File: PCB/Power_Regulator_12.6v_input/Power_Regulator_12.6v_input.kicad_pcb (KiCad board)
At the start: 2 copper layers, 90 x 90 mm, 53 parts, among them J1 SE2-30, U1 TLP3542, U2 TPS55340RTER, U3 TPS563203, U4 TPS54JA20RWWR

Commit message: added test points
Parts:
- added J10: Conn_01x01_Pin, TestPoint:TestPoint_Pad_D1.0mm, F.Cu at (142.4, 80.5)
- added J12: Conn_01x01_Pin, TestPoint:TestPoint_Pad_D1.0mm, F.Cu at (107.7, 95.7)
- added J13: Conn_01x01_Pin, TestPoint:TestPoint_Pad_D1.0mm, F.Cu at (114.5, 90.7)
- added J3: Conn_01x05_Pin, Connector_PinHeader_2.54mm:PinHeader_1x05_P2.54mm_Vertical, F.Cu at (178.5, 119.0)
- added J4: Conn_01x01_Pin, TestPoint:TestPoint_Pad_D1.0mm, F.Cu at (141.8, 73.4)
- added J5: Conn_01x01_Pin, TestPoint:TestPoint_Pad_D1.0mm, F.Cu at (150.0, 88.6)
- added J6: Conn_01x01_Pin, TestPoint:TestPoint_Pad_D1.0mm, F.Cu at (115.8, 107.0)
- added J7: Conn_01x01_Pin, TestPoint:TestPoint_Pad_D1.0mm, F.Cu at (120.0, 99.8)
- added J8: Conn_01x01_Pin, TestPoint:TestPoint_Pad_D1.0mm, F.Cu at (148.0, 68.2)
- added J9: Conn_01x01_Pin, TestPoint:TestPoint_Pad_D1.0mm, F.Cu at (151.4, 107.8)
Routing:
- net +5V: track 66.7 -> 151.0 mm
- net +BATT: track 95.0 -> 161.1 mm
- net /24V_RAW: track 24.1 -> 87.8 mm
- net +3.3VA: track 125.7 -> 170.5 mm
- net Net-(J12-Pin_1): track 3.46 -> 5.79 mm

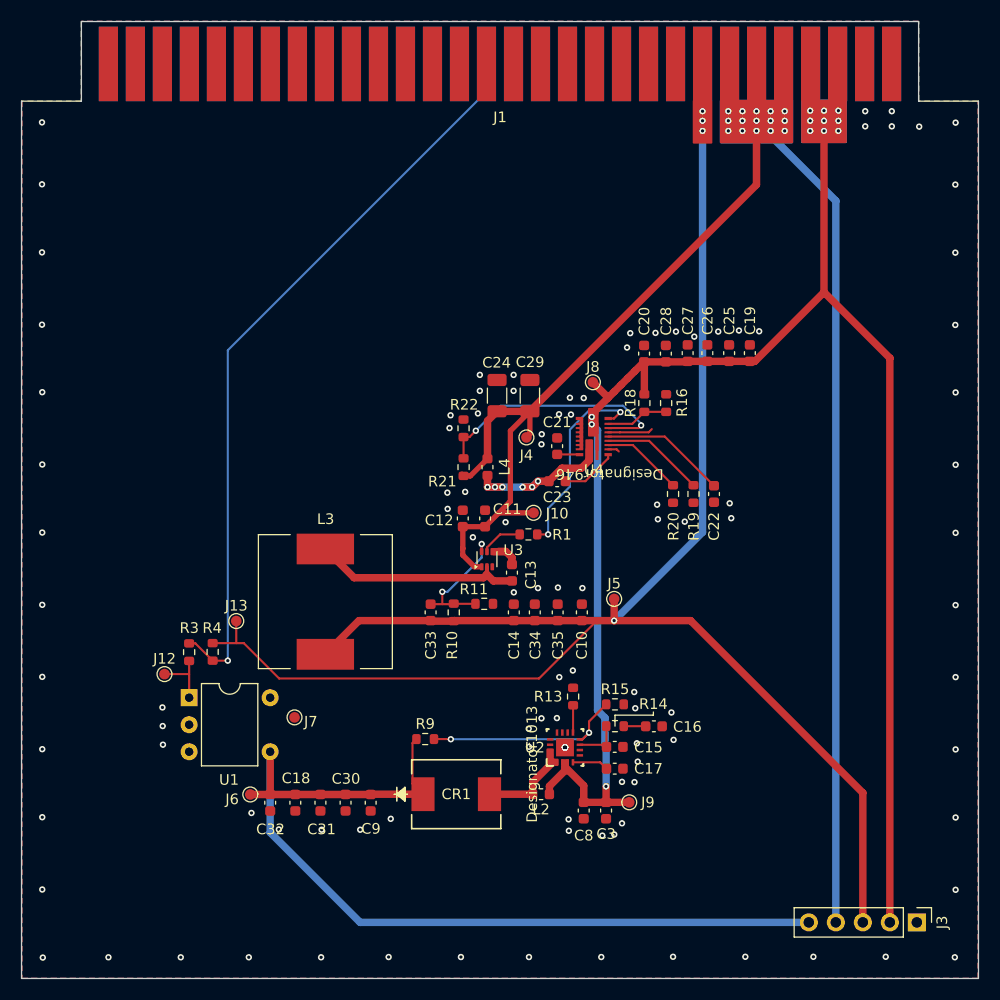
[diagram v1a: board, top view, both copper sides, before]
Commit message: added connector and switch
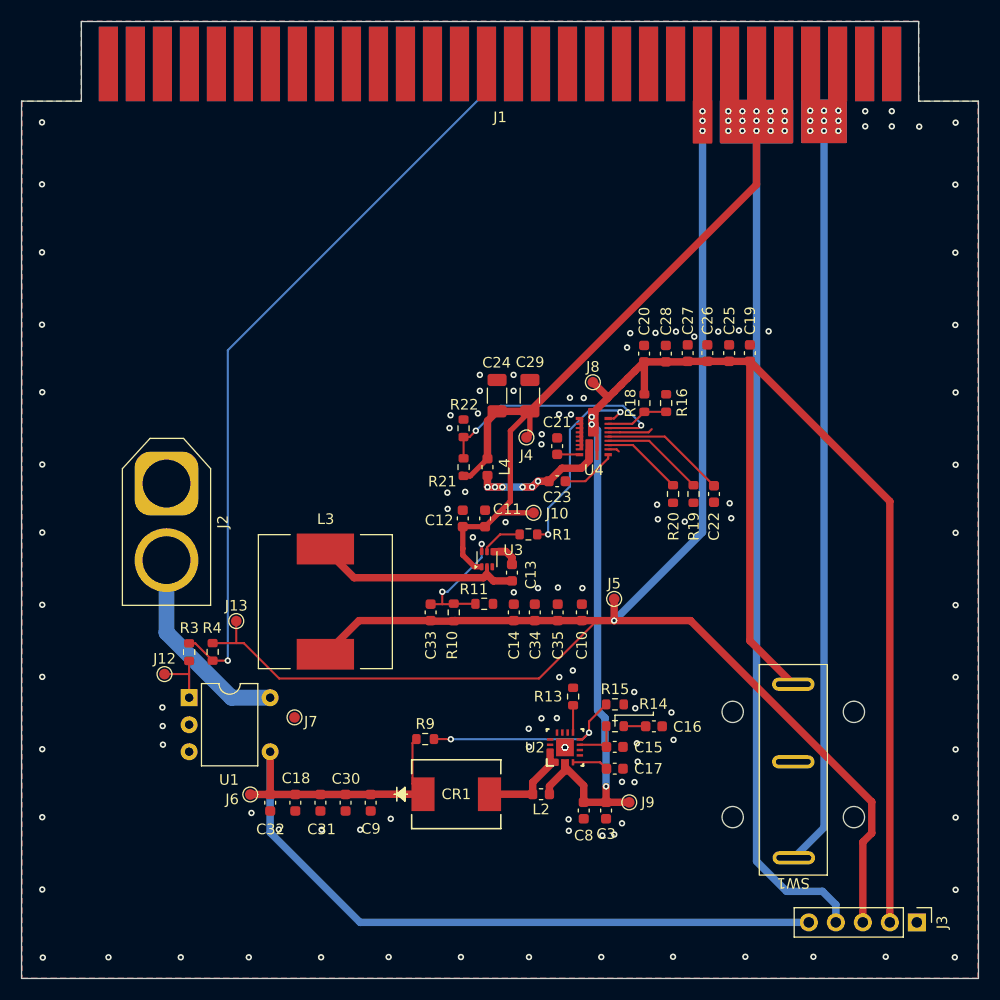
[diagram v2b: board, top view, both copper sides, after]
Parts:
- added J2: Jack-DC, XT-Conn:AMASS_XT60-M_1x02_P7.20mm_Vertical, F.Cu at (107.9, 77.8)
- added SW1: SW_SPDT_321, SS-5:SS-5, F.Cu at (170.1, 114.6)
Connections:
- J1 pad 27: +BATT -> /switch
- J1 pad 28: +BATT -> /switch
- J1 pad 57: +BATT -> /switch
- J1 pad 58: +BATT -> /switch
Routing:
- net /switch: track 0.00 -> 70.6 mm, vias 0 -> 9
- net +24V: track 0.00 -> 19.1 mm
- net +5V: track 151.0 -> 154.8 mm
- net +BATT: track 161.1 -> 162.7 mm, vias 12 -> 3
- net +3.3VA: track 170.5 -> 171.2 mm

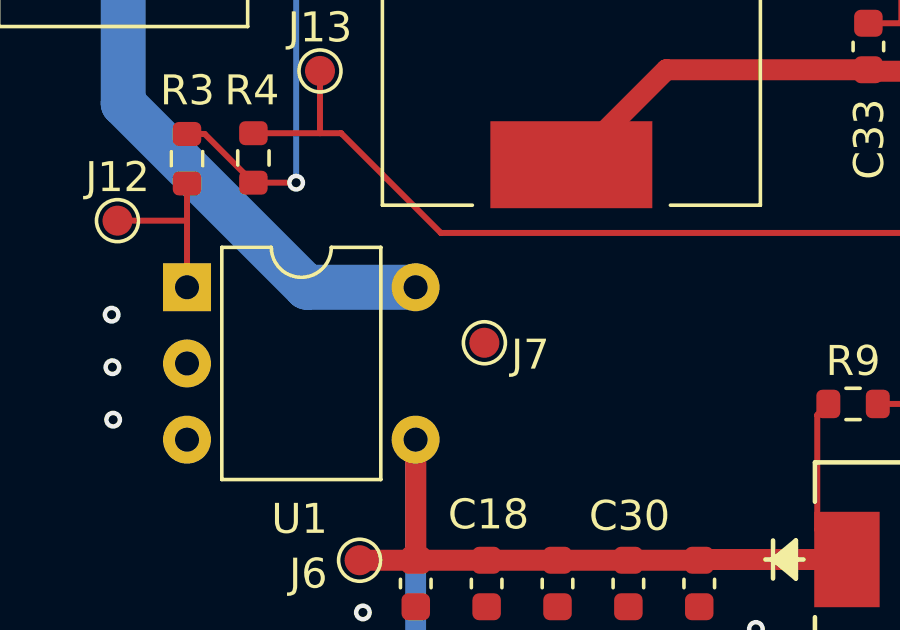
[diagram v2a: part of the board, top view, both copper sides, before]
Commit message: Fixed DRC error
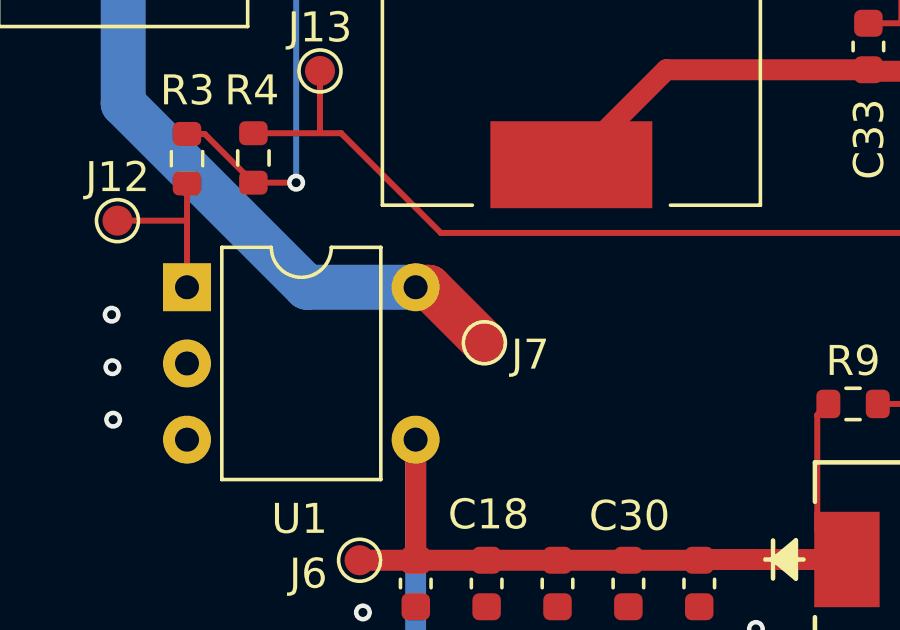
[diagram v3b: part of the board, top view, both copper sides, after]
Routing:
- net +24V: track 19.1 -> 22.2 mm
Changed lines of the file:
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@@
+	)
+	(segment
+		(start 117.6575 97.91)
+		(end 118.1 97.91)
+		(width 1.5)
+		(layer "F.Cu")
+		(net 71)
+	)
+	(segment
+		(start 118.1 97.91)
+		(end 119.95 99.76)
+		(width 1.5)
+		(layer "F.Cu")
+		(net 71)
 	)
 	(segment
